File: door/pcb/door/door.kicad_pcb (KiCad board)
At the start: 2 copper layers, 73.2 x 35.1 mm, 43 parts, among them J1 USB_B_Micro, J2 Conn_01x06_Male, J3 DB9_Female_MountingHoles, J4 Conn_01x03_Male, J5 Screw_Terminal_01x02, J6 Screw_Terminal_01x02, U1 10uF, U2 STM32F303CBTx, U3 SN65HVD230, Y1 8 Mhz

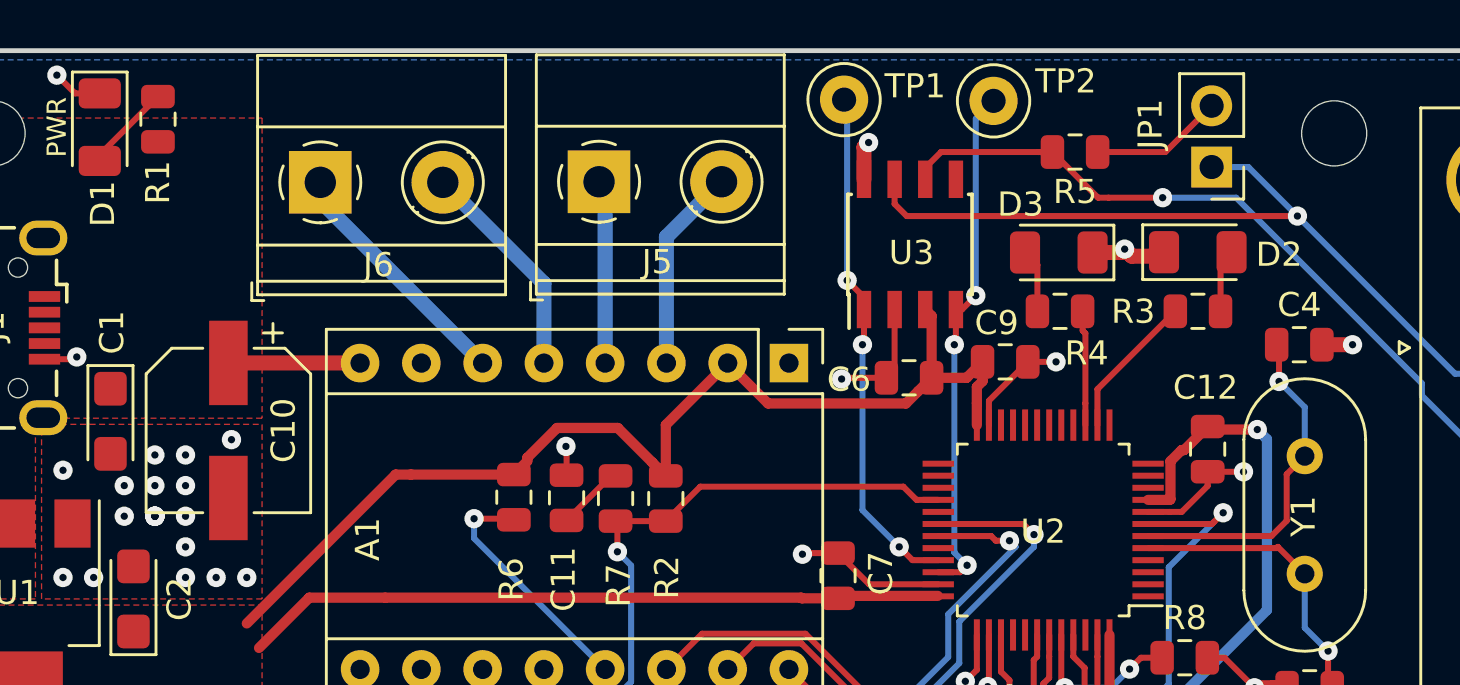
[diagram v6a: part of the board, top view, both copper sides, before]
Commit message: layout 100uF elko überarbeitet
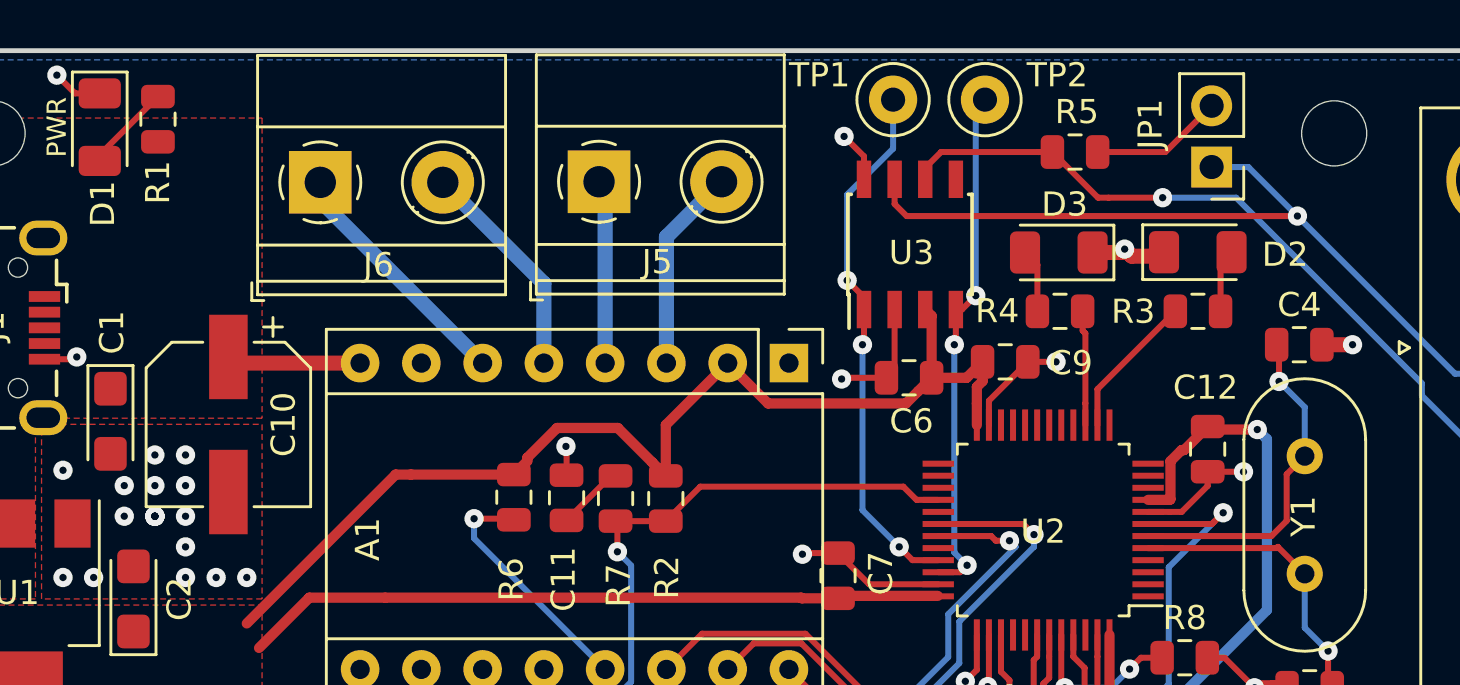
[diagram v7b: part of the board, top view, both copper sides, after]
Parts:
- moved TP1 2.03 mm to (190.0, 91.9)
- moved TP2 0.36 mm to (193.8, 91.9)
- moved C10 0.25 mm to (162.4, 105.4)
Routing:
- net CAN_RX: track 21.6 -> 22.6 mm
- net CAN_TX: track 21.4 -> 22.1 mm
- net GND: track 46.6 -> 47.1 mm, vias 33 -> 32
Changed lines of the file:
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@@
     (thickness 1.6)
     (drawings 25)
-    (tracks 343)
+    (tracks 345)
     (zones 0)
     (modules 43)
@@
   )
   (module Capacitor_SMD:CP_Elec_6.3x5.4 (layer F.Cu)
-    (at 162.433 105.664 270)
+    (at 162.433 105.416 270)
     (descr "SMT capacitor, aluminium electrolytic, 6.3x5.4, Panasonic C55 ")
     (tags "Capacitor Electrolytic")
@@
     (tags diode)
     (attr smd)
-    (fp_text reference D2 (at 3.3685 0.1016) (layer F.SilkS)
+    (fp_text reference D2 (at 3.6225 0.1016) (layer F.SilkS)
       (effects (font (size 1 1) (thickness 0.15)))
     )
@@
     (tags diode)
     (attr smd)
-    (fp_text reference D3 (at 1.5875 1.9939 180) (layer F.SilkS)
+    (fp_text reference D3 (at -0.2413 1.9939 180) (layer F.SilkS)
       (effects (font (size 1 1) (thickness 0.15)))
     )
@@
     (tags capacitor)
     (attr smd)
-    (fp_text reference C6 (at 2.4892 -0.0762 180) (layer F.SilkS)
+    (fp_text reference C6 (at -0.1016 -1.8034 180) (layer F.SilkS)
       (effects (font (size 1 1) (thickness 0.15)))
     )
@@
     (tags capacitor)
     (attr smd)
-    (fp_text reference C9 (at -0.3556 -1.6129) (layer F.SilkS)
+    (fp_text reference C9 (at 2.7178 0.0508) (layer F.SilkS)
       (effects (font (size 1 1) (thickness 0.15)))
     )
@@
     (tags resistor)
     (attr smd)
-    (fp_text reference R4 (at -1.1049 -1.7399 180) (layer F.SilkS)
+    (fp_text reference R4 (at 2.6035 0.0127 180) (layer F.SilkS)
       (effects (font (size 1 1) (thickness 0.15)))
     )
@@
     (tags resistor)
     (attr smd)
-    (fp_text reference R5 (at 0 -1.65 180) (layer F.SilkS)
+    (fp_text reference R5 (at -0.0762 1.6637 180) (layer F.SilkS)
       (effects (font (size 1 1) (thickness 0.15)))
     )
@@
   )
   (module TestPoint:TestPoint_Loop_D1.80mm_Drill1.0mm_Beaded (layer F.Cu)
-    (at 187.96 91.948)
+    (at 189.992 91.948)
     (descr "wire loop with bead as test point, loop diameter 1.8mm, hole diameter 1.0mm")
     (tags "test point wire loop bead")
-    (fp_text reference TP1 (at 2.9464 -0.5588) (layer F.SilkS)
+    (fp_text reference TP1 (at -3.048 -1.016) (layer F.SilkS)
       (effects (font (size 1 1) (thickness 0.15)))
     )
@@
   )
   (module TestPoint:TestPoint_Loop_D1.80mm_Drill1.0mm_Beaded (layer F.Cu)
-    (at 194.1576 91.9988)
+    (at 193.802 91.948)
     (descr "wire loop with bead as test point, loop diameter 1.8mm, hole diameter 1.0mm")
     (tags "test point wire loop bead")
-    (fp_text reference TP2 (at 2.9972 -0.8128) (layer F.SilkS)
+    (fp_text reference TP2 (at 2.9972 -1.016) (layer F.SilkS)
       (effects (font (size 1 1) (thickness 0.15)))
     )
@@
   (via (at 159.385 109.22) (size 0.8) (drill 0.3) (layers F.Cu B.Cu) (net 1))
   (via (at 159.385 109.22) (size 0.8) (drill 0.3) (layers F.Cu B.Cu) (net 1))
-  (via (at 188.976 93.726) (size 0.8) (drill 0.3) (layers F.Cu B.Cu) (net 1))
-  (segment (start 188.7855 95.25) (end 188.7855 93.9165) (width 0.625) (layer F.Cu) (net 1))
-  (segment (start 188.7855 93.9165) (end 188.976 93.726) (width 0.625) (layer F.Cu) (net 1))
   (segment (start 206.3265 116.332) (end 205.739 116.332) (width 0.625) (layer F.Cu) (net 1))
   (via (at 204.978 116.332) (size 0.8) (drill 0.3) (layers F.Cu B.Cu) (net 1))
@@
   (via (at 156.845 111.76) (size 0.8) (drill 0.3) (layers F.Cu B.Cu) (net 1))
   (via (at 155.575 107.315) (size 0.8) (drill 0.3) (layers F.Cu B.Cu) (net 1))
-  (via (at 162.56 106.045) (size 0.8) (drill 0.3) (layers F.Cu B.Cu) (net 1))
+  (via (at 187.96 93.472) (size 0.8) (drill 0.3) (layers F.Cu B.Cu) (net 1))
+  (segment (start 188.7855 95.25) (end 188.7855 94.2975) (width 0.25) (layer F.Cu) (net 1))
+  (segment (start 188.7855 94.2975) (end 187.96 93.472) (width 0.25) (layer F.Cu) (net 1))
   (segment (start 178.580299 105.559899) (end 180.012363 106.991963) (width 0.425) (layer F.Cu) (net 3))
   (segment (start 176.061439 105.559899) (end 178.580299 105.559899) (width 0.425) (layer F.Cu) (net 3))
@@
   (segment (start 195.55899 118.51201) (end 196.223799 117.847201) (width 0.25) (layer F.Cu) (net 9))
   (segment (start 196.223799 116.159439) (end 196.465 115.918238) (width 0.25) (layer F.Cu) (net 9))
-  (segment (start 167.888 102.864) (end 167.894 102.87) (width 0.25) (layer F.Cu) (net 10))
-  (segment (start 162.433 102.864) (end 167.888 102.864) (width 0.625) (layer F.Cu) (net 10))
+  (segment (start 167.888 102.864) (end 167.894 102.87) (width 0.625) (layer F.Cu) (net 10))
+  (segment (start 162.687 102.87) (end 162.433 102.616) (width 0.625) (layer F.Cu) (net 10))
+  (segment (start 167.894 102.87) (end 162.687 102.87) (width 0.625) (layer F.Cu) (net 10))
   (segment (start 185.674 115.57) (end 189.23 119.126) (width 0.25) (layer F.Cu) (net 11))
   (segment (start 197.933401 115.509901) (end 197.465 115.0415) (width 0.25) (layer F.Cu) (net 11))
@@
   (segment (start 188.722 108.966) (end 190.246 110.49) (width 0.25) (layer B.Cu) (net 51))
   (segment (start 188.722 102.108) (end 188.722 108.966) (width 0.25) (layer B.Cu) (net 51))
-  (segment (start 188.087 92.075) (end 187.96 91.948) (width 0.25) (layer B.Cu) (net 51))
-  (segment (start 188.087 99.441) (end 188.087 92.075) (width 0.25) (layer B.Cu) (net 51))
+  (segment (start 188.087 99.441) (end 188.087 95.885) (width 0.25) (layer B.Cu) (net 51))
+  (segment (start 189.992 93.98) (end 189.992 91.948) (width 0.25) (layer B.Cu) (net 51))
+  (segment (start 188.087 95.885) (end 189.992 93.98) (width 0.25) (layer B.Cu) (net 51))
   (via (at 192.532 102.108) (size 0.8) (drill 0.3) (layers F.Cu B.Cu) (net 52))
   (segment (start 192.5955 100.65) (end 192.5955 102.0445) (width 0.25) (layer F.Cu) (net 52))
@@
   (segment (start 192.847 100.65) (end 193.421 100.076) (width 0.25) (layer F.Cu) (net 52))
   (segment (start 193.421 92.7354) (end 194.1576 91.9988) (width 0.25) (layer B.Cu) (net 52))
-  (segment (start 193.421 100.076) (end 193.421 92.7354) (width 0.25) (layer B.Cu) (net 52))
+  (segment (start 193.421 92.329) (end 193.802 91.948) (width 0.25) (layer B.Cu) (net 52))
+  (segment (start 193.421 100.076) (end 193.421 92.329) (width 0.25) (layer B.Cu) (net 52))
   (via (at 192.988418 116.065798) (size 0.8) (drill 0.3) (layers F.Cu B.Cu) (net 53))
   (segment (start 193.465 114.1415) (end 193.465 115.589216) (width 0.25) (layer F.Cu) (net 53))
